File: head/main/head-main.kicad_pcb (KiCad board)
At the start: 4 copper layers, 30 x 20 mm, 77 parts, among them J1 conn_head_b, U1 CV1800B, U2 AR0237CS, U3 GTA2718B-3HA, U4 W25Q128JVP, U5 RP509x, U6 RP509x, U7 RP114x, U8 LP3982S, U9 NCP136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

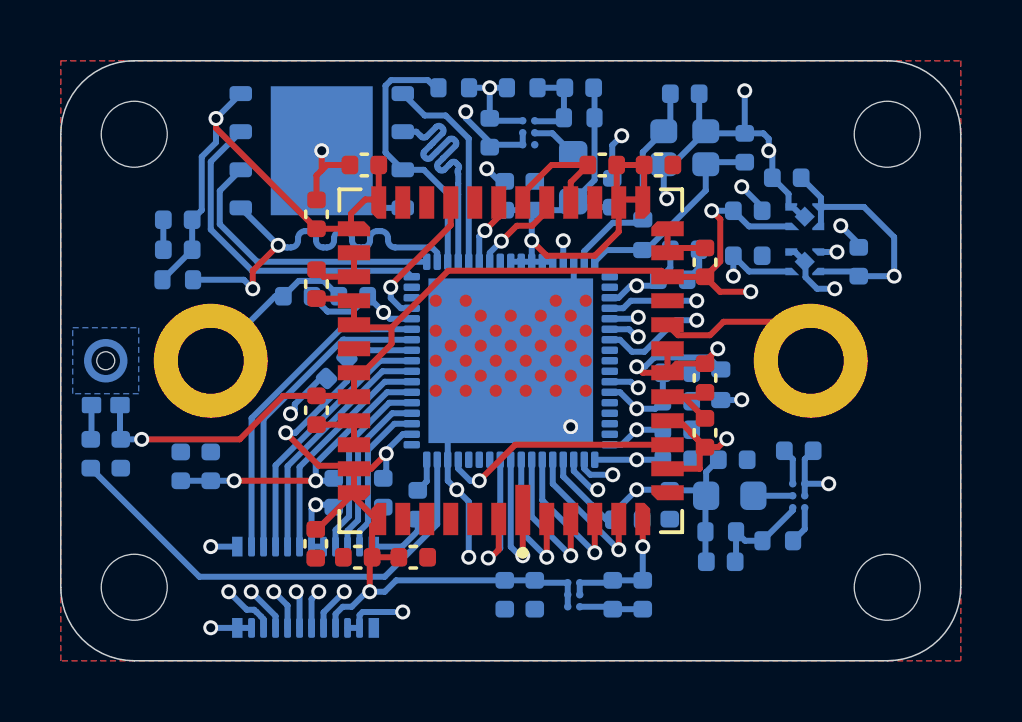
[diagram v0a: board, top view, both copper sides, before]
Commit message: update communication pinout
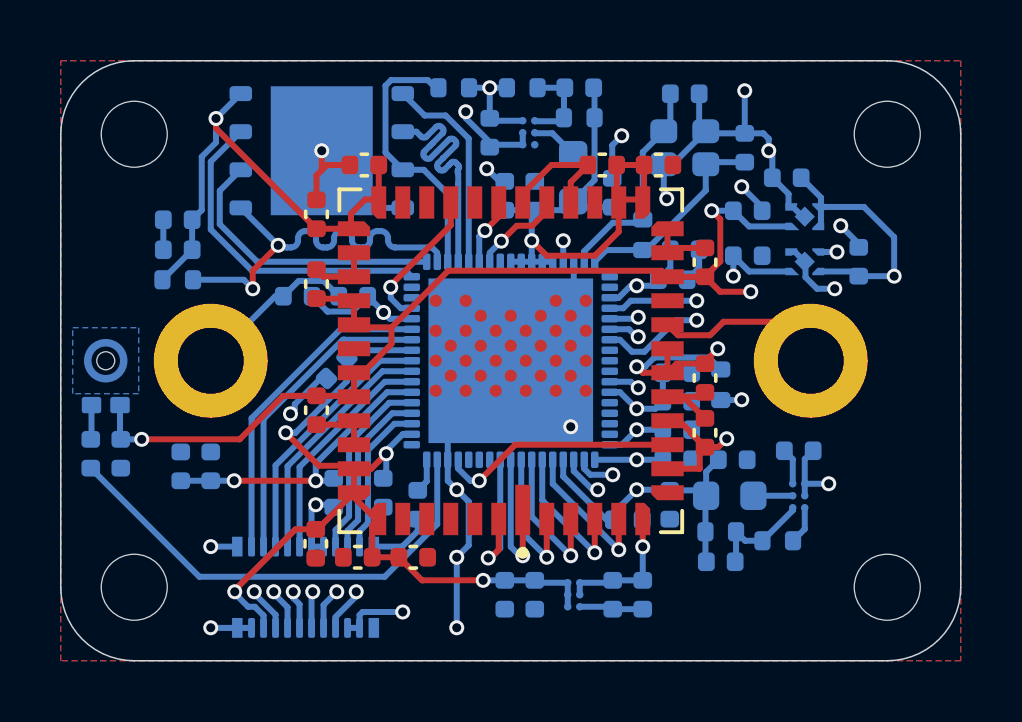
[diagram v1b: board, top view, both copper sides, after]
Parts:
- J1: value conn_head_b -> conn_head_comms
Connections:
- net /U3CTS renamed /UDIR
- J1 pad 10: /USB_DP -> /LED
- J1 pad 12: /U3TX -> /U3RX
- J1 pad 14: /U3RX -> /U3TX
- J1 pad 18: /U3RTS -> +1V8
- J1 pad 6: +1V8 -> /USB_DM
- J1 pad 8: /USB_DM -> /USB_DP
- U1 pad 41: /U3RTS -> /LED
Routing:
- net /U3RTS: track 27.6 -> 0.00 mm, vias 2 -> 0
- net /LED: track 0.00 -> 21.4 mm, vias 0 -> 2
- net GND: track 73.0 -> 75.5 mm, vias 17 -> 18
- net +1V8: track 107.5 -> 109.3 mm, vias 8 -> 9
- net /UDIR: track 24.3 -> 23.4 mm
- net /U3RX: track 18.1 -> 17.5 mm

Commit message: finishing touches
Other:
- board text added: "NAFCDP"

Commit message: larger traces
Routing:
- net +1V8: track 109.3 -> 110.8 mm
- net +5V: track 57.1 -> 55.7 mm
- added copper zone on B.Cu, net +1V8
- added copper zone on B.Cu, net +5V
- added copper zone on B.Cu, net Net-(U5-LX)
- added copper zone on B.Cu, net Net-(U6-LX)
